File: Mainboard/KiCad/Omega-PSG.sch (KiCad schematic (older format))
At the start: 14 parts, among them J7 JOYSTICK_A, J8 JOYSTICK_B, U28 74HCT157, U29 74HCT157, U35 74HCT74, U36 74HCT74, U39 74AHCT32, U4 YM2149, U42 74LS07, U44 74AHCT02

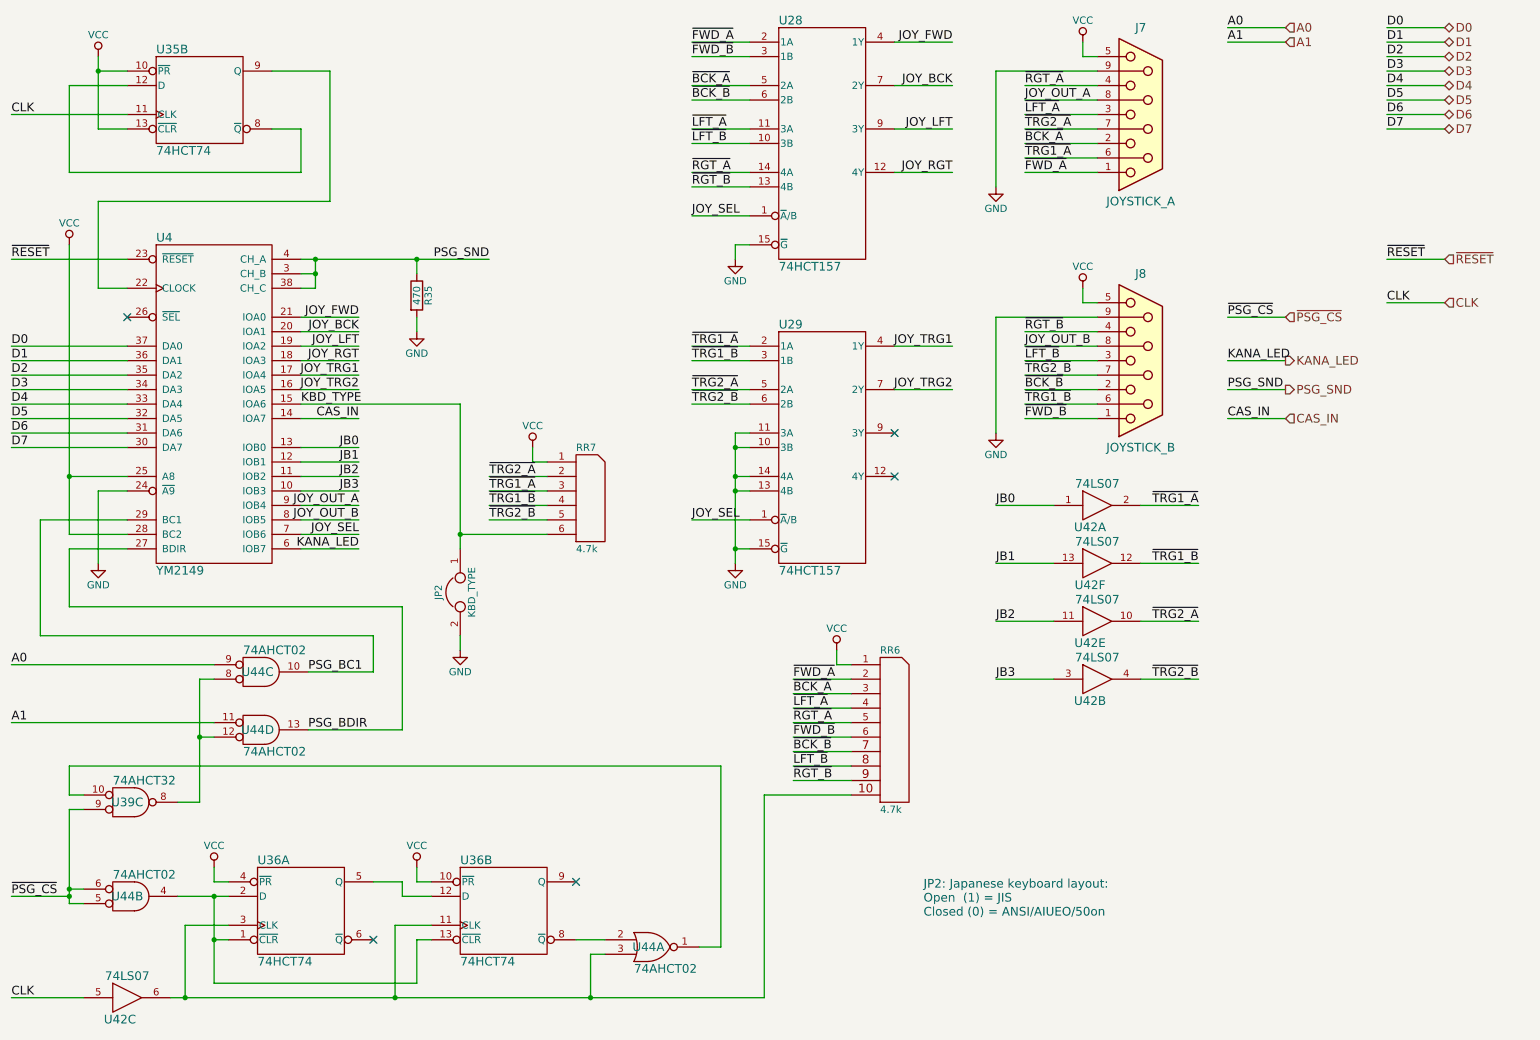
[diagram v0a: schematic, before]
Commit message: Mainboard: Fix some of the issues described in #1
Signed-off-by: Sergey Kiselev <skiselev@gmail.com>
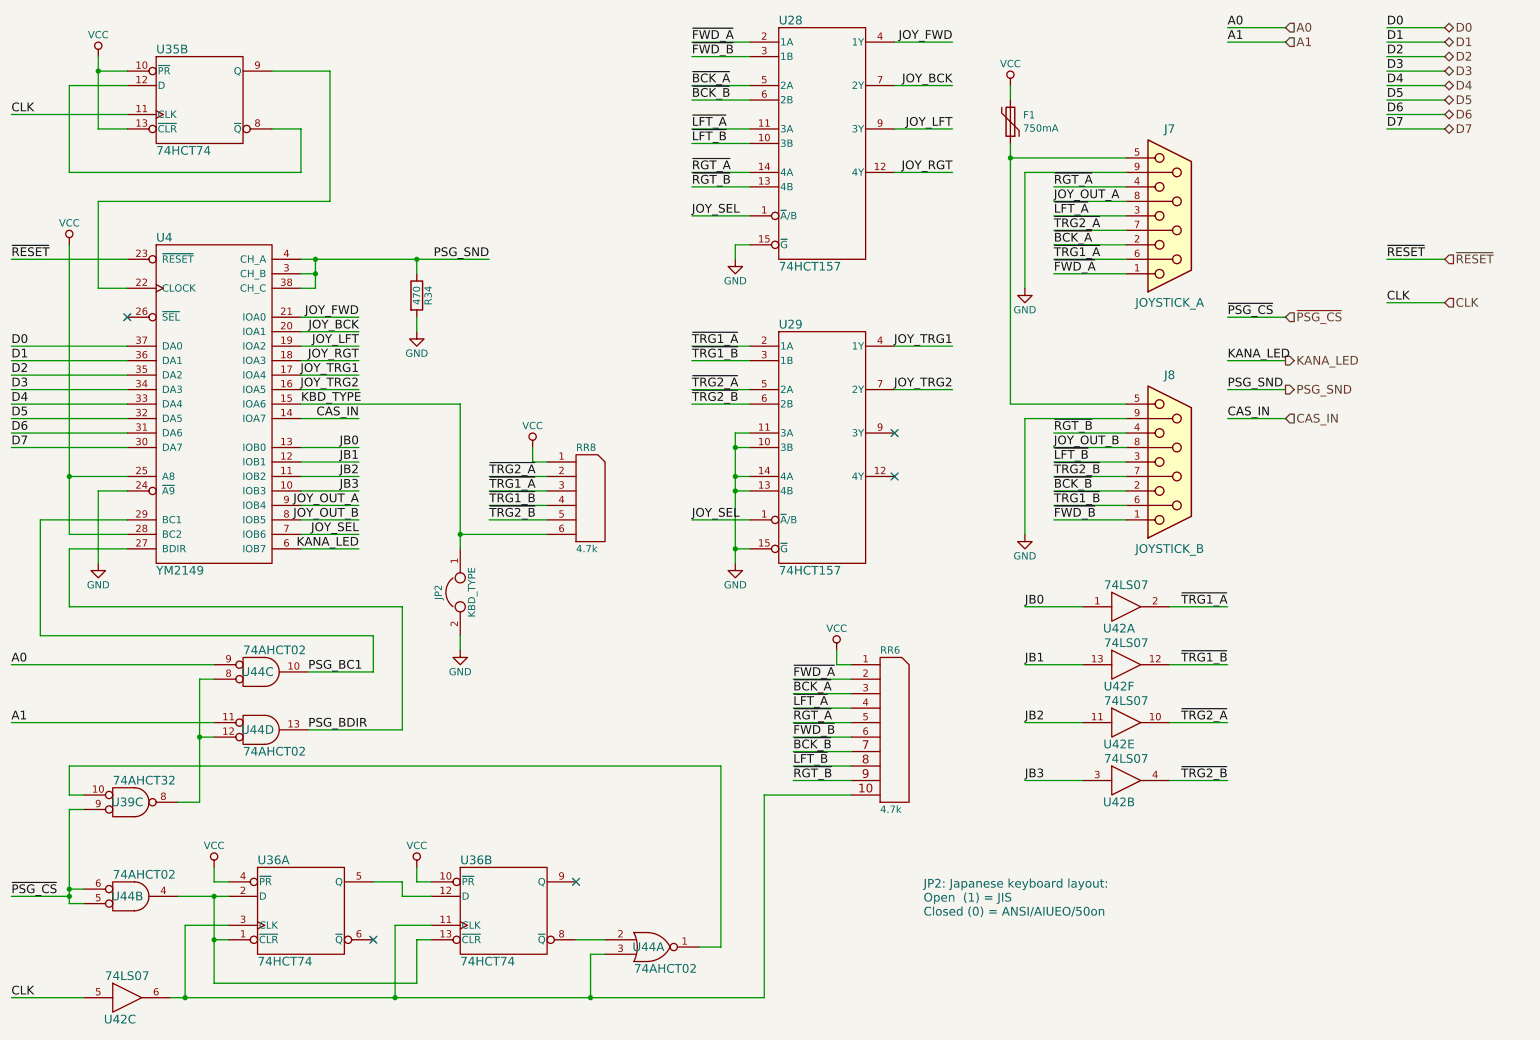
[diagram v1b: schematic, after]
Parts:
- added F1: 750mA, My_Components:Cap_Cer_508, symbol Device:Polyfuse
- renumbered R35 to R34, RR7 to RR8
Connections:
- net VCC: now also F1.2; no longer J7.5, J8.5
- new net: F1.1, J7.5, J8.5
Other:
- moved on the sheet: J7, J8, U42A, U42B, U42E, U42F
